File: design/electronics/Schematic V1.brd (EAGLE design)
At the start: 160 x 100 mm, 174 parts, among them J1 PJ-202AH, J2 PJ-025, J3 DD50P564GTXLF, J4 DD50P564GTXLF, J5 SAMTEC-TST-105-01-X-DJ, J6 SSW-106-02-TM-S-RA, SW1 TL6330AF200Q, U1 STM32F207VGT6TR, U10 SN65LBC175ADD16-M, U11 TPSC107K010R0200TPSC107K010R0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, U12 SN75ALS174ADWRDW20-M, U13 SN75468DRD0016A_M, U14 SN75468DRD0016A_M, U15 ACSL-6400-00TESOIC_6400-00TE-M, U16 ACSL-6400-00TESOIC_6400-00TE-M, U17 SN65LBC175ADD16-M, U18 SN65LBC175ADD16-M, U19 SN65LBC175ADD16-M, U2 LM2678S-5.0/NOPBTS7B-M, U20 TPSC107K010R0200TPSC107K010R0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, U21 TPSC107K010R0200TPSC107K010R0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, U22 TPSC107K010R0200TPSC107K010R0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, U23 TPSC107K010R0200TPSC107K010R0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, U24 TPSC107K010R0200TPSC107K010R0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, U3 VS-6TQ045S-M3DPAK_045S-M3_VIS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, U4 LM2678S-3.3/NOPBTS7B-M, U5 STM32F207VGT6TR, U6 VS-6TQ045S-M3DPAK_045S-M3_VIS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, U7 SN75ALS174ADWRDW20-M, U8 OPA4205APWRTSSOP14_PW_R-PDSO-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, U9 TPS63700DRCR

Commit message: Updated Schematic, board layout, BOM, and libraries
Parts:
- removed C10: GRM2195C1H103JA01DG-21_MUR-M, SSW-130-01-G-S:G-21_MUR-M
- removed C11, C12: TR3E156M050C0300CAP_TR3E_VIS-M, SSW-130-01-G-S:CAP_TR3E_VIS-M
- removed C13: 293D474X9050B2TE3CAP_293D_B_VIS-M, SSW-130-01-G-S:CAP_293D_B_VIS-M
- added C5, C6: 1.0uF, SparkFun-Capacitors:0805
- added H1, H2, H3, H4: MOUNT-HOLE4.1, holes:4,1
- added L5: BLM21PG600SN1DIND_BLM21_MUR-M, SSW-130-01-G-S:IND_BLM21_MUR-M
- L2: value 2300HT-220-H-RC -> BLM21PG600SN1DIND_BLM21_MUR-M; device SSW-130-01-G-S:IND_2300HT-H_118_66 -> SSW-130-01-G-S:IND_BLM21_MUR-M
- U21, U22, U24: value TPSC107K010R0200TPSC107K010R0200_AVX-M -> RS0104YQTSSOP-14_JRT-M; device SSW-130-01-G-S:TPSC107K010R0200_AVX-M -> SSW-130-01-G-S:TSSOP-14_JRT-M
- U4: value LM2678S-3.3/NOPBTS7B-M -> TLV1117LV33DCYR; device SSW-130-01-G-S:TS7B-M -> SSW-130-01-G-S:VREG_TLV1117LV33DCYR
- U6: value VS-6TQ045S-M3DPAK_045S-M3_VIS-M -> RS0104YQTSSOP-14_JRT-M; device SSW-130-01-G-S:DPAK_045S-M3_VIS-M -> SSW-130-01-G-S:TSSOP-14_JRT-M
- moved C4 347.9 mm to (41.1, 82.5), turned to 90 degrees
- moved C3 334.6 mm to (34.3, 83.8), turned to 90 degrees
- moved C2 319.2 mm to (26.7, 83.8), turned to 90 degrees
- moved U6 283.9 mm to (-241.3, -132.1)
- moved U21 256.0 mm to (-241.3, -156.2), flipped to the top, turned to 0 degrees
- moved U4 170.1 mm to (83.8, 49.5)
- moved L2 155.1 mm to (-242.6, -24.1)
- moved U22 110.5 mm to (-241.3, -108.0)
- moved U24 88.9 mm to (-241.3, -180.3)
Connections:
- removed net N$1: C10.1, U4.3
- removed net SWITCH_OUT_3.3V: C10.2, L2.1, U4.1, U6.2
- new net ABS_ENC_OUT_GPIO_1_5V: U10.13, U21.5
- new net ABS_ENC_OUT_GPIO_2_5V: U17.13, U24.5
- new net ENC_PUL_OUT_A_GPIO_1_5V: U10.3, U21.2
- new net ENC_PUL_OUT_A_GPIO_2_5V: U17.3, U24.2
- new net ENC_PUL_OUT_B_GPIO_1_5V: U10.5, U21.3
- new net ENC_PUL_OUT_B_GPIO_2_5V: U17.5, U24.3
- new net ENC_PUL_OUT_C_GPIO_1_5V: U10.11, U21.4
- new net ENC_PUL_OUT_C_GPIO_2_5V: U17.11, U24.4
- new net GEN_PURPOSE_OUT_GPIO_A_1_5V: U18.3, U22.2
- new net GEN_PURPOSE_OUT_GPIO_A_2_5V: U6.2
- new net GEN_PURPOSE_OUT_GPIO_B_1_5V: U18.5, U22.3
- new net GEN_PURPOSE_OUT_GPIO_B_2_5V: U6.3
- new net GEN_PURPOSE_OUT_GPIO_C_1_5V: U18.11, U22.4
- new net GEN_PURPOSE_OUT_GPIO_C_2_5V: U6.4
- new net N$14: C32.2, C33.2, L5.1, U5.22
- new net SERVO_ALARM_OUT_GPIO_1_5V: U18.13, U22.5
- new net SERVO_ALARM_OUT_GPIO_2_5V: U6.5
- new net S_GNDA: L2.2, U5.20
- net +14V: no longer C11.1, C12.1, C13.1, U4.2
- net +3.3V: now also C6.1, L5.2, U21.14, U22.14, U24.14, U4.2, U4.4, U6.14; no longer C32.2, C33.2, L2.2, U21.2, U22.2, U24.2, U4.6, U5.22
- net +5V: now also C5.1, U21.1, U21.8, U22.1, U22.8, U24.1, U24.8, U4.3, U6.1, U6.8
- net ABS_ENC_OUT_GPIO_1: now also U21.10; no longer U10.13
- net ABS_ENC_OUT_GPIO_2: now also U24.10; no longer U17.13
- net ENC_PUL_OUT_A_GPIO_1: now also U21.13; no longer U10.3
- net ENC_PUL_OUT_A_GPIO_2: now also U24.13; no longer U17.3
- net ENC_PUL_OUT_B_GPIO_1: now also U21.12; no longer U10.5
- net ENC_PUL_OUT_B_GPIO_2: now also U24.12; no longer U17.5
- net ENC_PUL_OUT_C_GPIO_1: now also U21.11; no longer U10.11
- net ENC_PUL_OUT_C_GPIO_2: now also U24.11; no longer U17.11
- net GEN_PURPOSE_OUT_GPIO_A_1: now also U22.13; no longer U18.3
- net GEN_PURPOSE_OUT_GPIO_A_2: now also U6.13
- net GEN_PURPOSE_OUT_GPIO_B_1: now also U22.12; no longer U18.5
- net GEN_PURPOSE_OUT_GPIO_B_2: now also U6.12
- net GEN_PURPOSE_OUT_GPIO_C_1: now also U22.11; no longer U18.11
- net GEN_PURPOSE_OUT_GPIO_C_2: now also U6.11
- net P_GND: now also C5.2, C6.2, U4.1; no longer C11.2, C12.2, C13.2, U21.1, U22.1, U24.1, U4.4, U4.8, U6.1, U6.3
- net SERVO_ALARM_OUT_GPIO_1: now also U22.10; no longer U18.13
- net SERVO_ALARM_OUT_GPIO_2: now also U6.10
- net S_GND: now also L2.1, U21.7, U22.7, U24.7, U6.7; no longer U5.20
- net V_ON: no longer U4.7

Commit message: Updated layout parts
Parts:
- removed U20, U23: TPSC107K010R0200TPSC107K010R0200_AVX-M, SSW-130-01-G-S:TPSC107K010R0200_AVX-M
- C1: value TR3E156M050C0300CAP_TR3E_VIS-M -> 0.1uF; device SSW-130-01-G-S:CAP_TR3E_VIS-M -> SparkFun-Capacitors:0805
- C2: value TR3E156M050C0300CAP_TR3E_VIS-M -> 20SVPF180MPCAP_SVP_E7_PAN-M; device SSW-130-01-G-S:CAP_TR3E_VIS-M -> SSW-130-01-G-S:PCAP_SVP_E7_PAN-M
- C3: value TR3E156M050C0300CAP_TR3E_VIS-M -> 10SVPC330MCAP_SVPC_E7_PAN-M; device SSW-130-01-G-S:CAP_TR3E_VIS-M -> SSW-130-01-G-S:CAP_SVPC_E7_PAN-M
- C4: value 293D474X9050B2TE3CAP_293D_B_VIS-M -> 10pF; device SSW-130-01-G-S:CAP_293D_B_VIS-M -> SparkFun-Capacitors:0805
- L1: value 2300HT-220-H-RC -> SRP1270-100MIND_BOURNS_SRP1270-M; device SSW-130-01-G-S:IND_2300HT-H_118_66 -> SSW-130-01-G-S:IND_BOURNS_SRP1270-M
- U11: value TPSC107K010R0200TPSC107K010R0200_AVX-M -> MAX7375AXR805+T21-0075D_MXM-M; device SSW-130-01-G-S:TPSC107K010R0200_AVX-M -> SSW-130-01-G-S:21-0075D_MXM-M
- U3: value VS-6TQ045S-M3DPAK_045S-M3_VIS-M -> CDBC520-GCDBC-G-M; device SSW-130-01-G-S:DPAK_045S-M3_VIS-M -> SSW-130-01-G-S:CDBC-G-M
- moved C4 533.9 mm to (-256.5, -360.7), turned to 0 degrees
- moved U11 519.7 mm to (-243.8, -344.2)
- moved R19 32.0 mm to (59.8, 87.4), turned to 270 degrees
- moved C3 30.7 mm to (64.8, 80.0), flipped to the bottom
- moved C5 27.3 mm to (63.5, 54.6)
- moved C1 22.7 mm to (41.8, 84.3), turned to 270 degrees
- moved LED1 21.8 mm to (59.8, 82.7), turned to 180 degrees
- moved C6 20.4 mm to (68.3, 47.6), turned to 90 degrees
- moved U4 20.3 mm to (63.5, 49.5), turned to 270 degrees
- moved U3 17.8 mm to (36.8, 84.5), flipped to the bottom
- moved L1 8.98 mm to (52.1, 68.6), flipped to the top, turned to 0 degrees
- moved C2 4.56 mm to (27.7, 88.3)
- moved R1 1.25 mm to (57.4, 82.5), turned to 90 degrees
- moved R2 0.25 mm to (57.4, 86.4)
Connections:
- new net EXT_CLK: U11.2
- new net N$1: U1.12
- net +14V: now also C1.2; no longer C1.1, C3.1, C4.1
- net +3.3V: now also C4.2, U11.1
- net +5V: now also C3.1; no longer U11.2, U20.2, U23.2
- net P_GND: now also C1.1, U3.2; no longer C1.2, C4.2, U11.1, U20.1, U23.1, U3.1, U3.3
- net SWITCH_OUT_5V: now also U3.1; no longer U3.2
- net S_GND: now also C4.1, U11.3
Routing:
- net +5V: track 44.5 -> 5.33 mm
- net P_GND: track 17.5 -> 26.6 mm, vias 12 -> 6
- net SWITCH_OUT_5V: track 0.00 -> 5.22 mm, vias 0 -> 1
- net N$22: track 5.67 -> 2.70 mm
- net +3.3V: track 0.00 -> 2.90 mm
- net V_ON: track 7.83 -> 6.72 mm
- net +14V: track 9.45 -> 10.3 mm
- added copper zone on layer 1, net +3.3V

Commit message: Updated Power Circuit Schematic + Layout + Components
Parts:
- removed C37: 10uF, SparkFun-Capacitors:0805
- removed C38: 0.1uF, rcl:C0805
- removed C39: 4.7nF, rcl:C0805
- removed C40: 10pF, SparkFun-Capacitors:0805
- removed C41, C42, C43, C44: 4.7uF, rcl:C0805
- removed C45: (no value), rcl:C0805
- removed CR1: SL03-GS18CR_SL03_VIS-M, SSW-130-01-G-S:CR_SL03_VIS-M
- removed R6: 100k, rcl:R0805
- removed U9: TPS63700DRCR, SSW-130-01-G-S:DRC10_2P4X1P65
- added C10: 2.2uF, SparkFun-Capacitors:0805
- added C11: 470nF, SparkFun-Capacitors:0805
- added C12, C9: 4.7uF, SparkFun-Capacitors:0805
- added C13: 120pF, SparkFun-Capacitors:0805
- added C14: 10uF, SparkFun-Capacitors:0805
- added C8: 68uF, SSW-130-01-G-S:PCAP_6.3X7.7-ELECT_NCA-M
- L3: value 7443551131IND_1365-WE-HCI_WRE-M -> 22uH; device SSW-130-01-G-S:IND_1365-WE-HCI_WRE-M -> SSW-130-01-G-S:IND_VLS201610CX-220M-1
- R3: value 10 -> 105k
- R4: value 1.5M -> 73.2k
- R5: value 121k -> 1M
- R69: value (none) -> 10k
- U5: value STM32F207VGT6TR -> LM43601PWPRPWP16_TEX-M; device SSW-130-01-G-S:LQFP100-14X14MM -> SSW-130-01-G-S:PWP16_TEX-M
- moved C4 405.6 mm to (-83.8, 6.35)
- moved U11 405.6 mm to (-71.1, 22.9)
- moved R4 345.0 mm to (25.4, 50.8), turned to 90 degrees
- moved LED2 295.8 mm to (12.4, 39.4), turned to 270 degrees
- moved R3 290.6 mm to (20.2, 44.3), turned to 90 degrees
- moved R20 260.1 mm to (11.4, 45.7), turned to 270 degrees
- moved R5 233.5 mm to (25.4, 56.5), turned to 90 degrees
- moved L3 231.7 mm to (12.4, 49.5)
- moved U1 193.1 mm to (-66.0, -5.08)
- moved U5 102.8 mm to (17.8, 50.8), turned to 90 degrees
- moved C3 19.7 mm to (45.1, 80.0)
- moved C5 17.8 mm to (45.7, 54.6)
- moved U4 17.8 mm to (45.7, 49.5)
- moved C6 17.8 mm to (50.5, 47.6)
- moved R1 16.5 mm to (40.9, 82.5)
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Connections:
- removed net FRWD_EX_TORQUE_LIM_GPIO_1: U1.63
- removed net FRWD_EX_TORQUE_LIM_GPIO_2: U1.70
- removed net GND: R20.1
- removed net N$10: C40.2, R4.2, R5.1, U9.9
- removed net N$6: C38.1, R3.1, U9.3, U9.4
- removed net N$9: C45.1, R5.2, U9.10
- removed net VBAT: U1.6
- removed net VCAP_1: U1.49
- removed net VCAP_2: U1.73
- removed net VDD: U1.100
- removed net VDDA: U1.22
- removed net VDD_2: U1.11
- removed net VDD_3: U1.19
- removed net VDD_4: U1.28
- removed net VDD_5: U1.50
- removed net VDD_6: U1.75
- removed net VREF+: U1.21
- removed net VSS: U1.74
- removed net VSSA: U1.20
- removed net VSS_2: U1.10
- removed net VSS_3: U1.27
- new net SW_OUT: C11.1, L3.2, U5.1, U5.2
- net +14V: now also C8.1, C9.2, U5.12, U5.13, U5.14
- net +3.3V: now also U1.100, U1.11, U1.19, U1.21, U1.28, U1.50, U1.6, U1.75; no longer U5.100, U5.11, U5.19, U5.21, U5.28, U5.50, U5.6, U5.75
- net +5V: no longer C37.2, R3.2, U9.5
- net -15V: now also C10.1, C12.1, C14.1, C9.1, U5.10, U5.15, U5.16, U5.EPAD; no longer C41.1, C42.1, C43.1, C44.1, CR1.2, R6.2, U9.8
- net EXT_CLK: now also U1.12
- net FRWD_EX_TORQUE_LIM_EN_GPIO_1: now also U1.63
- net FRWD_EX_TORQUE_LIM_EN_GPIO_2: now also U1.70
- net GEN_PURPOSE_OUT_GPIO_A_2: no longer U19.3
- net GEN_PURPOSE_OUT_GPIO_A_2_5V: now also U19.3
- net GEN_PURPOSE_OUT_GPIO_B_2: no longer U19.5
- net GEN_PURPOSE_OUT_GPIO_B_2_5V: now also U19.5
- net GEN_PURPOSE_OUT_GPIO_C_2: no longer U19.11
- net GEN_PURPOSE_OUT_GPIO_C_2_5V: now also U19.11
- net N$1: now also C10.2, U5.4; no longer U1.12
- net N$11: now also C13.1, R4.2, R5.1, U5.9; no longer C40.1, R6.1
- net N$14: now also U1.22; no longer U5.22
- net N$3: now also C11.2, U5.3; no longer C39.1, U9.1
- net N$4: now also U1.49; no longer U5.49
- net N$5: now also U1.73; no longer U5.73
- net N$7: now also R3.2, U5.8; no longer CR1.1, L3.2, U9.6
- net P_GND: now also C12.2, C13.2, C14.2, C8.2, R20.1, R3.1, R5.2, U5.5; no longer C37.1, C38.2, C39.2, C41.2, C42.2, C43.2, C44.2, C45.2, U9.2, U9.7
- net SERVO_ALARM_OUT_GPIO_2: no longer U19.13
- net SERVO_ALARM_OUT_GPIO_2_5V: now also U19.13
- net S_GND: now also U1.10, U1.27, U1.74; no longer U5.10, U5.27, U5.74
- net S_GNDA: now also U1.20; no longer U5.20
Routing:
- net N$11: track 0.00 -> 10.6 mm
- net P_GND: track 26.6 -> 35.2 mm, vias 6 -> 10
- net +14V: track 10.3 -> 17.2 mm, vias 2 -> 4
- net N$23: track 0.00 -> 5.41 mm
- net N$1: track 0.00 -> 5.28 mm
- net N$3: track 0.00 -> 5.14 mm
- net N$7: track 0.00 -> 2.61 mm
- net -15V: track 0.00 -> 1.77 mm, vias 0 -> 1
- added copper zone on layer 1, net -15V
- added copper zone on layer 1, net SW_OUT

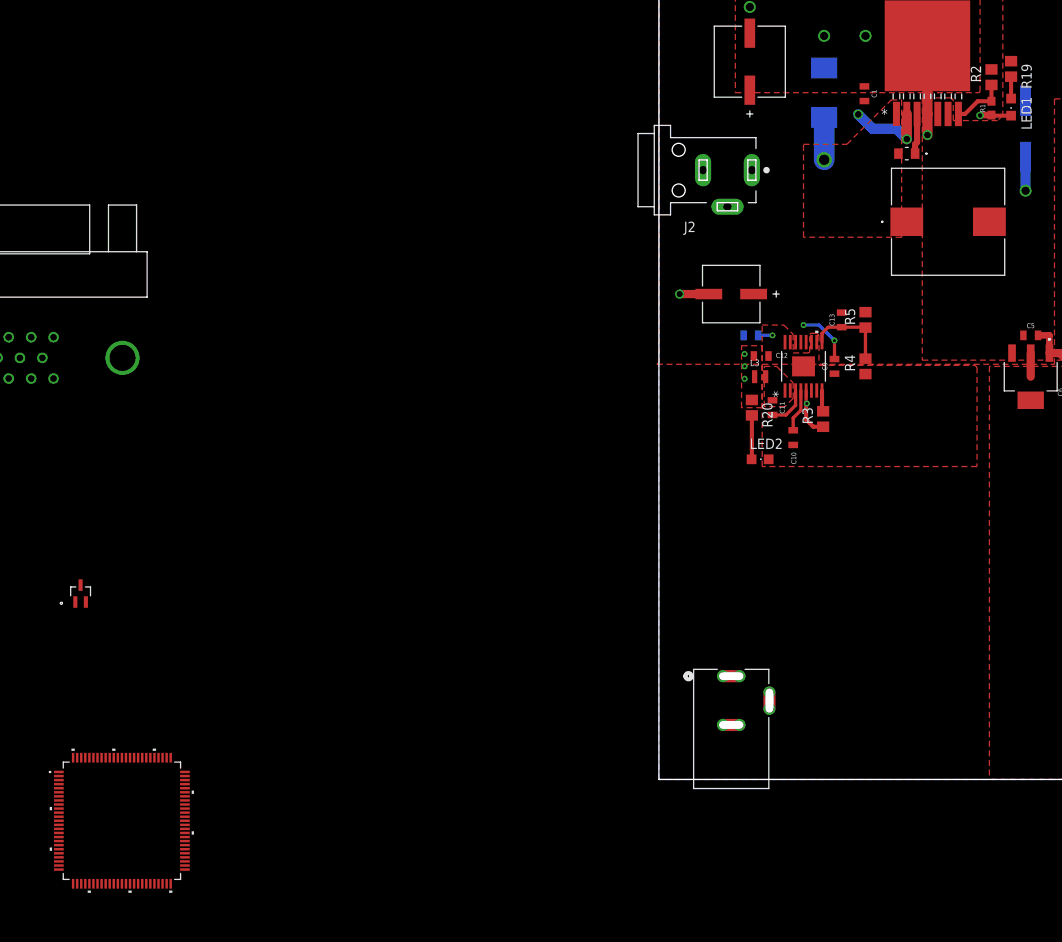
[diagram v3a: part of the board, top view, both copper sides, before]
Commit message: Updated Schematic and Board with a few components
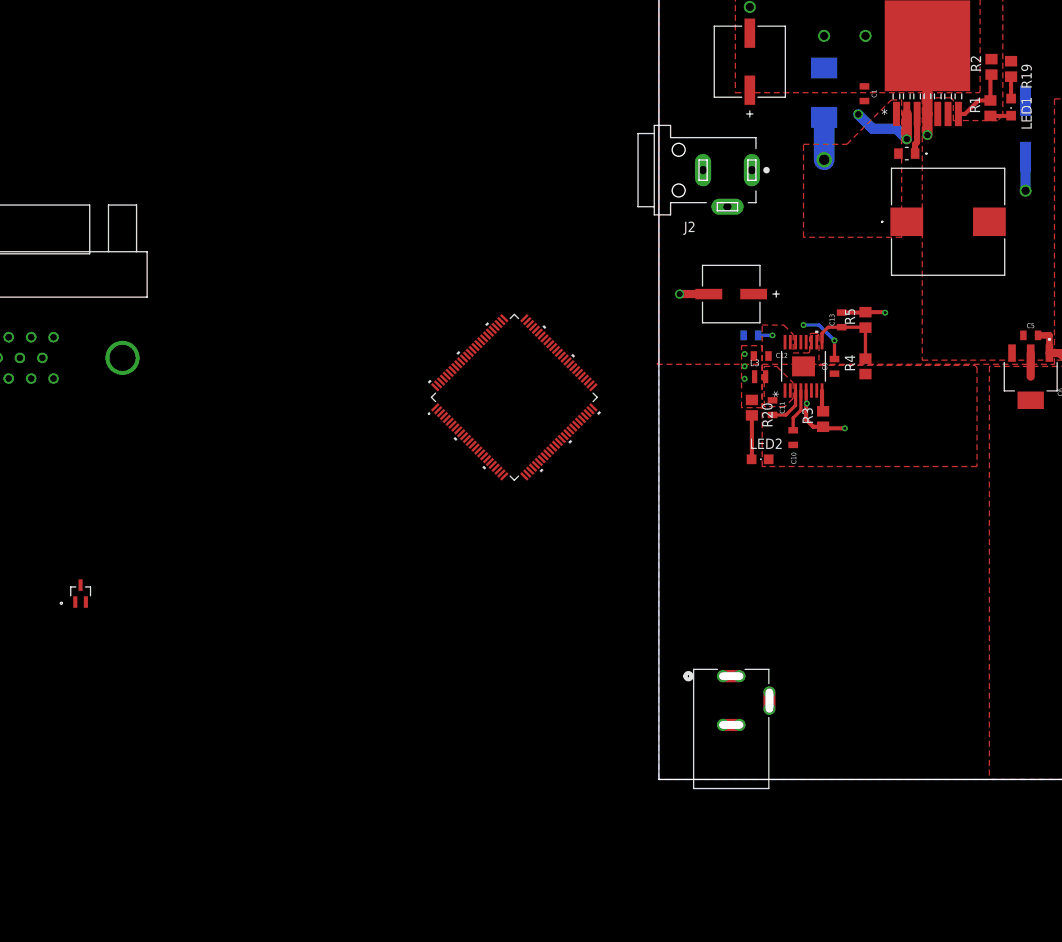
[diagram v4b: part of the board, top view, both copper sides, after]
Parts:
- R1: device SparkFun-Resistors:0603 -> rcl:R0805
- moved U1 71.0 mm to (-17.8, 47.0), turned to 45 degrees
- moved R2 1.27 mm to (40.9, 87.6)
- moved R1 0.13 mm to (40.8, 82.5)
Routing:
- net P_GND: track 35.2 -> 42.0 mm, vias 10 -> 11
- net V_ON: track 6.72 -> 7.86 mm

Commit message: Updated Power Scheme of STM32
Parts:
- moved C35 420.8 mm to (87.9, 27.6), flipped to the bottom, turned to 180 degrees
- moved C36 416.6 mm to (86.7, 38.2), flipped to the bottom, turned to 270 degrees
- moved C34 414.6 mm to (95.2, 42.9), turned to 270 degrees
- moved C33 406.1 mm to (81.9, 34.0), flipped to the bottom, turned to 270 degrees
- moved C32 401.3 mm to (79.6, 34.0), flipped to the bottom, turned to 270 degrees
- moved C29 397.5 mm to (78.4, 24.6), flipped to the bottom, turned to 180 degrees
- moved C31 395.2 mm to (72.9, 30.7), flipped to the bottom, turned to 180 degrees
- moved C27 390.9 mm to (94.4, 45.5), turned to 180 degrees
- moved C30 388.5 mm to (72.9, 36.6), flipped to the bottom, turned to 180 degrees
- moved C28 386.8 mm to (83.1, 42.5), flipped to the bottom, turned to 90 degrees
- moved C23 382.4 mm to (88.5, 33.0), flipped to the bottom, turned to 270 degrees
- moved C26 382.3 mm to (85.0, 42.5), flipped to the bottom, turned to 90 degrees
- moved C22 381.2 mm to (90.8, 33.0), flipped to the bottom, turned to 270 degrees
- moved C25 380.7 mm to (83.1, 38.2), flipped to the bottom, turned to 270 degrees
- moved C24 378.1 mm to (87.1, 42.5), flipped to the bottom, turned to 90 degrees
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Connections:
- net N$14 renamed +3.3VA
- net S_GND: no longer C32.1, C33.1
- net S_GNDA: now also C32.1, C33.1
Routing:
- net +3.3V: track 2.90 -> 96.4 mm, vias 0 -> 13
- net S_GND: track 0.00 -> 76.7 mm, vias 0 -> 8
- net S_GNDA: track 0.00 -> 7.74 mm, vias 0 -> 1
- net +3.3VA: track 0.00 -> 7.06 mm, vias 0 -> 1
- net P_GND: track 42.0 -> 48.6 mm, vias 11 -> 12
- net N$4: track 0.00 -> 3.01 mm, vias 0 -> 1
- net N$5: track 0.00 -> 2.87 mm
- net SWITCH_OUT_5V: track 5.22 -> 8.07 mm
- added copper zone on layer 16, net +3.3V
- added copper zone on layer 16, net S_GND

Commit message: Updated Schematic Layout
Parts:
- moved U22 361.8 mm to (96.5, 21.6), turned to 90 degrees
- moved U11 22.1 mm to (74.4, 37.7), turned to 0 degrees
- moved C20 1.27 mm to (72.9, 40.0)
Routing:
- net EXT_CLK: track 0.00 -> 2.80 mm
- net S_GND: track 76.7 -> 79.3 mm
- net +3.3V: track 96.4 -> 98.9 mm

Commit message: Updated Layout with most ICs on board now
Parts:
- moved H1 582.2 mm to (30.5, 306.1)
- moved H2 582.2 mm to (30.5, 295.9)
- moved H3 582.2 mm to (30.5, 285.8)
- moved H4 582.2 mm to (30.5, 275.6)
- moved J5 475.6 mm to (213.4, 102.9)
- moved U24 448.8 mm to (94.4, 117.6), turned to 180 degrees
- moved U21 429.5 mm to (94.4, 111.8), turned to 180 degrees
- moved U6 391.3 mm to (90.4, 75.4), turned to 90 degrees
- moved U14 346.7 mm to (114.6, 93.5)
- moved J4 345.7 mm to (160.0, 109.0), turned to 270 degrees
- moved U13 333.0 mm to (114.6, 82.2)
- moved U18 327.9 mm to (85.1, 61.6), turned to 180 degrees
- moved U12 308.8 mm to (115.6, 64.5)
- moved U8 288.5 mm to (31.8, 92.7)
- moved U17 281.1 mm to (82.5, 154.7)
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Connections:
- net ABS_ENC_OUT_GPIO_1: now also U1.83; no longer U1.1
- net ABS_ENC_OUT_GPIO_2: now also U1.87; no longer U1.5
- net ALARM_RST_GPIO_1: now also U1.60; no longer U1.62
- net ALARM_RST_GPIO_2: now also U1.67; no longer U1.69
- net ALO_GPIO_A_1: now also U1.32; no longer U1.33
- net ALO_GPIO_B_1: now also U1.33; no longer U1.34
- net ALO_GPIO_C_1: now also U1.34; no longer U1.32
- net ENC_PUL_OUT_A_GPIO_1: now also U1.80; no longer U1.96
- net ENC_PUL_OUT_A_GPIO_2: now also U1.84; no longer U1.2
- net ENC_PUL_OUT_B_GPIO_1: now also U1.81; no longer U1.97
- net ENC_PUL_OUT_B_GPIO_2: now also U1.85; no longer U1.3
- net ENC_PUL_OUT_C_GPIO_1: now also U1.82; no longer U1.98
- net ENC_PUL_OUT_C_GPIO_2: now also U1.86; no longer U1.4
- net FRWD_DRIVE_EN_GPIO_1: now also U1.62; no longer U1.60
- net FRWD_DRIVE_EN_GPIO_2: now also U1.69; no longer U1.67
- net FRWD_EX_TORQUE_LIM_EN_GPIO_1: now also U1.59; no longer U1.63
- net FRWD_EX_TORQUE_LIM_EN_GPIO_2: now also U1.66; no longer U1.70
- net PROP_CONTROL_EN_GPIO_1: now also U1.63; no longer U1.59
- net PROP_CONTROL_EN_GPIO_2: now also U1.70; no longer U1.66
- net REVERSE_EX_TORQUE_LIM_EN_GPIO_1: now also U1.58; no longer U1.64
- net REVERSE_EX_TORQUE_LIM_EN_GPIO_2: now also U1.65; no longer U1.71
- net SERVO_EN_GPIO_1: now also U1.64; no longer U1.58
- net SERVO_EN_GPIO_2: now also U1.71; no longer U1.65
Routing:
- net CLR_GPIO_1: track 0.00 -> 64.5 mm
- net DIR_GPIO_1: track 0.00 -> 64.5 mm
- net POS_EN_GPIO: track 0.00 -> 59.9 mm, vias 0 -> 4
- net TORQUE-SPEED_DAC_1: track 0.00 -> 55.8 mm, vias 0 -> 3
- net CLR_GPIO_2: track 0.00 -> 49.2 mm
- net TORQUE-SPEED_DAC_2: track 0.00 -> 48.6 mm, vias 0 -> 3
- net PULSE_GPIO_1: track 0.00 -> 48.3 mm
- net DIR_GPIO_2: track 0.00 -> 46.6 mm
- net S_GND: track 79.3 -> 124.2 mm, vias 8 -> 13
- net PULSE_GPIO_2: track 0.00 -> 32.0 mm
- net ALO_GPIO_A_1: track 0.00 -> 25.7 mm
- net REVERSE_EX_TORQUE_LIM_EN_GPIO_1: track 0.00 -> 25.1 mm
- net FRWD_EX_TORQUE_LIM_EN_GPIO_1: track 0.00 -> 24.8 mm
- net ALO_GPIO_B_1: track 0.00 -> 24.7 mm
- net ALARM_RST_GPIO_1: track 0.00 -> 24.5 mm
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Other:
- board size 160 x 100 mm -> 160 x 149.2 mm

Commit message: More of the layout is added
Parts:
- moved R30 391.6 mm to (77.1, 33.7), flipped to the bottom, turned to 270 degrees
- moved R29 383.5 mm to (73.4, 33.7), flipped to the bottom, turned to 270 degrees
- moved R28 375.5 mm to (69.7, 33.7), flipped to the bottom, turned to 270 degrees
- moved R27 367.5 mm to (66.0, 33.7), flipped to the bottom, turned to 270 degrees
- moved R18 359.5 mm to (62.1, 33.7), flipped to the bottom, turned to 270 degrees
- moved R17 351.5 mm to (58.0, 33.7), flipped to the bottom, turned to 270 degrees
- moved D6 316.1 mm to (78.2, 37.8)
- moved R69 313.3 mm to (62.7, 64.3), turned to 180 degrees
- moved D5 310.2 mm to (74.5, 37.8)
- moved D4 304.4 mm to (70.9, 37.8)
- moved R68 303.7 mm to (67.1, 43.8), flipped to the bottom, turned to 180 degrees
- moved R65 299.6 mm to (79.0, 43.6), flipped to the bottom, turned to 180 degrees
- moved D3 298.9 mm to (67.2, 37.8)
- moved R67 297.0 mm to (62.2, 43.8), flipped to the bottom
- moved D2 293.5 mm to (63.2, 37.8)
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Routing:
- net S_GND: track 124.2 -> 404.7 mm, vias 13 -> 33
- net +5V: track 5.33 -> 183.7 mm, vias 1 -> 14
- net SWCLK: track 0.00 -> 92.9 mm, vias 0 -> 1
- net SWDIO: track 0.00 -> 92.9 mm, vias 0 -> 1
- net +3.3V: track 103.3 -> 192.9 mm, vias 12 -> 24
- net NRST: track 12.1 -> 99.1 mm, vias 0 -> 1
- net UART_TX: track 0.00 -> 69.3 mm, vias 0 -> 1
- net UART_RX: track 0.00 -> 67.8 mm, vias 0 -> 2
- net +24V: track 0.00 -> 64.4 mm, vias 0 -> 2
- net P_GND: track 48.6 -> 77.0 mm, vias 12 -> 17
- net N$13: track 0.00 -> 28.0 mm
- net GEN_PURPOSE_OUT_GPIO_C_2_5V: track 0.00 -> 22.1 mm
- net GEN_PURPOSE_OUT_GPIO_B_2_5V: track 0.00 -> 21.3 mm
- net GEN_PURPOSE_OUT_GPIO_C_1_5V: track 0.00 -> 20.0 mm
- net GEN_PURPOSE_OUT_GPIO_B_1_5V: track 0.00 -> 19.6 mm
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- added copper zone on layer 1, net +24V
- added copper zone on layer 16, net +24V
- added copper zone on layer 1, net 1.65V_REF
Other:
- board size 160 x 149.2 mm -> 152.4 x 149.3 mm
